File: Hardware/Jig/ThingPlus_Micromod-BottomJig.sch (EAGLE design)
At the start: 41 parts, among them J1 USB_A_PTH_MALE, J5 USB_A_SMT_FEMALE, J7 QWIIC_RIGHT_ANGLE, U1 TB_MAIN_BRAIN_CARDEDGE_TB_SIDE, U2 74LVC4066, U4 74LVC4066_MUX_1:1_X4

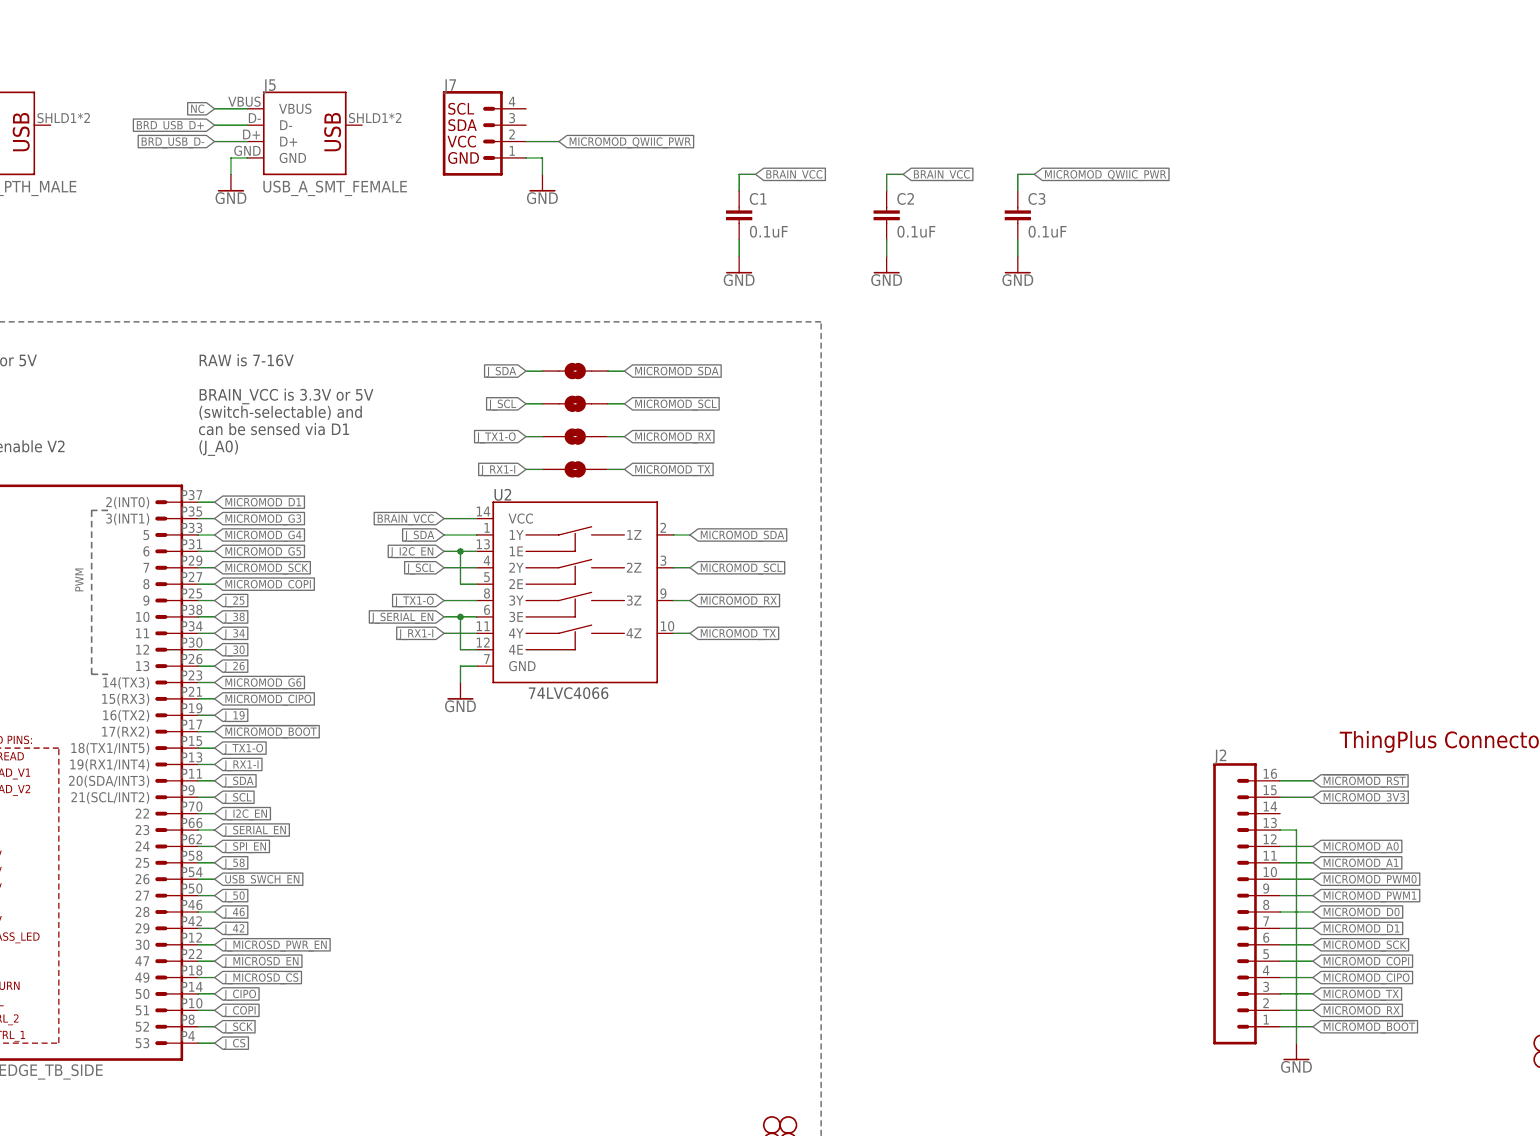
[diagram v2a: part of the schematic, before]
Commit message: Updated board and middle jig
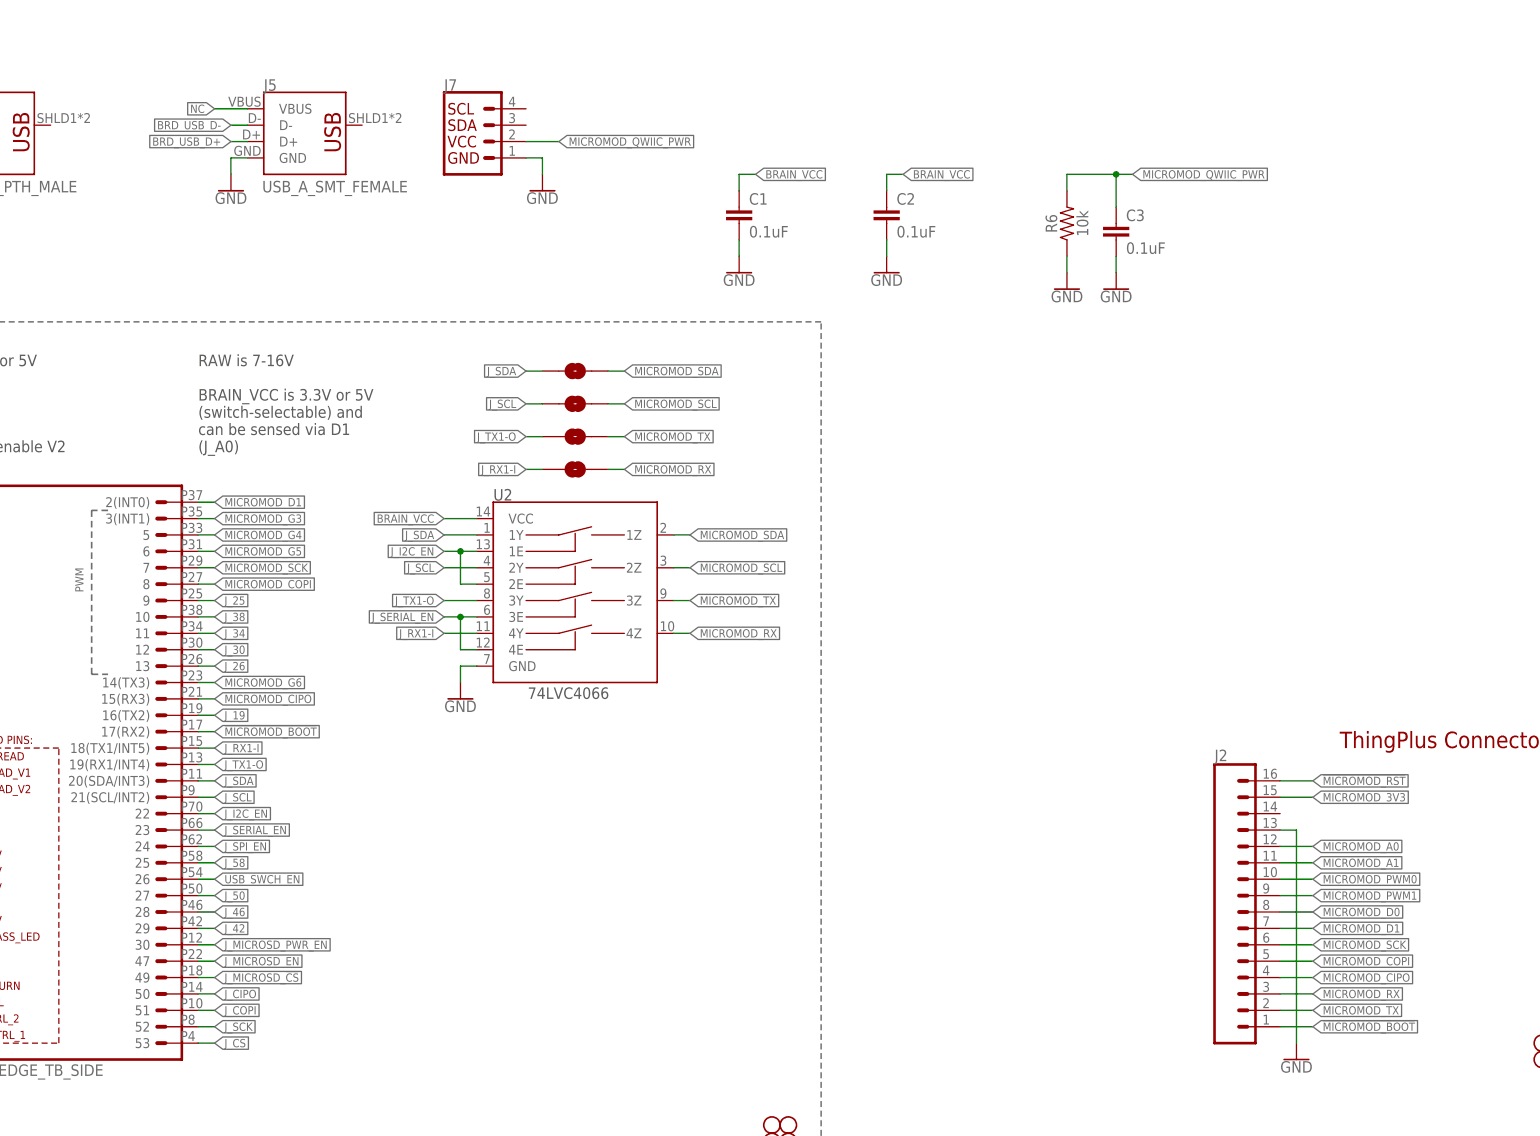
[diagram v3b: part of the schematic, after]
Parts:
- added R6: 10k, SparkFun-Resistors:10KOHM-0603-1/10W-1%
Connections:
- net BRD_USB_D+: now also J5.D+; no longer J5.D-
- net BRD_USB_D-: now also J5.D-; no longer J5.D+
- net GND: now also R6.1
- net J_RX1-I: now also U1.18(TX1/INT5); no longer U1.19(RX1/INT4)
- net J_TX1-O: now also U1.19(RX1/INT4); no longer U1.18(TX1/INT5)
- net MICROMOD_QWIIC_PWR: now also R6.2
- net MICROMOD_RX: now also J2.3, J_SDA.2, U2.4Z; no longer J2.2, J_SCL1.2, U2.3Z
- net MICROMOD_TX: now also J2.2, J_SCL1.2, U2.3Z; no longer J2.3, J_SDA.2, U2.4Z
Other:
- moved on the sheet: C3
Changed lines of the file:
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@@
 <part name="GND8" library="SparkFun-PowerSymbols" deviceset="GND" device=""/>
 <part name="H5" library="SparkFun-Hardware" deviceset="STAND-OFF" device=""/>
+<part name="R6" library="SparkFun-Resistors" deviceset="10KOHM" device="-0603-1/10W-1%" value="10k"/>
+<part name="GND9" library="SparkFun-PowerSymbols" deviceset="GND" device=""/>
 </parts>
 <sheets>
@@
 <attribute name="VALUE" x="264.16" y="187.706" size="1.778" layer="96" align="top-center"/>
 </instance>
-<instance part="C3" gate="G$1" x="284.48" y="195.58" smashed="yes">
-<attribute name="NAME" x="286.004" y="198.501" size="1.778" layer="95" font="vector"/>
-<attribute name="VALUE" x="286.004" y="193.421" size="1.778" layer="96" font="vector"/>
-</instance>
-<instance part="GND8" gate="1" x="284.48" y="187.96" smashed="yes">
-<attribute name="VALUE" x="284.48" y="187.706" size="1.778" layer="96" align="top-center"/>
+<instance part="C3" gate="G$1" x="299.72" y="193.04" smashed="yes">
+<attribute name="NAME" x="301.244" y="195.961" size="1.778" layer="95" font="vector"/>
+<attribute name="VALUE" x="301.244" y="190.881" size="1.778" layer="96" font="vector"/>
+</instance>
+<instance part="GND8" gate="1" x="299.72" y="185.42" smashed="yes">
+<attribute name="VALUE" x="299.72" y="185.166" size="1.778" layer="96" align="top-center"/>
 </instance>
 <instance part="H5" gate="G$1" x="246.38" y="55.88" smashed="yes"/>
+<instance part="R6" gate="G$1" x="292.1" y="195.58" smashed="yes" rot="R90">
+<attribute name="NAME" x="290.576" y="195.58" size="1.778" layer="95" font="vector" rot="R90" align="bottom-center"/>
+<attribute name="VALUE" x="293.624" y="195.58" size="1.778" layer="96" font="vector" rot="R90" align="top-center"/>
+</instance>
+<instance part="GND9" gate="1" x="292.1" y="185.42" smashed="yes">
+<attribute name="VALUE" x="292.1" y="185.166" size="1.778" layer="96" align="top-center"/>
+</instance>
 </instances>
 <busses>
@@
 <segment>
 <pinref part="C3" gate="G$1" pin="2"/>
-<wire x1="284.48" y1="193.04" x2="284.48" y2="190.5" width="0.1524" layer="91"/>
+<wire x1="299.72" y1="190.5" x2="299.72" y2="187.96" width="0.1524" layer="91"/>
 <pinref part="GND8" gate="1" pin="GND"/>
+</segment>
+<segment>
+<wire x1="292.1" y1="190.5" x2="292.1" y2="187.96" width="0.1524" layer="91"/>
+<pinref part="GND9" gate="1" pin="GND"/>
+<pinref part="R6" gate="G$1" pin="1"/>
 </segment>
 </net>
@@
 </segment>
 <segment>
-<label x="160.02" y="111.76" size="1.27" layer="95" xref="yes"/>
-<pinref part="U1" gate="G$1" pin="19(RX1/INT4)"/>
-<wire x1="157.48" y1="111.76" x2="160.02" y2="111.76" width="0.1524" layer="91"/>
+<pinref part="U1" gate="G$1" pin="18(TX1/INT5)"/>
+<wire x1="157.48" y1="114.3" x2="160.02" y2="114.3" width="0.1524" layer="91"/>
+<label x="160.02" y="114.3" size="1.27" layer="95" xref="yes"/>
 </segment>
 </net>
@@
 </segment>
 <segment>
-<label x="160.02" y="114.3" size="1.27" layer="95" xref="yes"/>
-<pinref part="U1" gate="G$1" pin="18(TX1/INT5)"/>
-<wire x1="157.48" y1="114.3" x2="160.02" y2="114.3" width="0.1524" layer="91"/>
+<pinref part="U1" gate="G$1" pin="19(RX1/INT4)"/>
+<wire x1="157.48" y1="111.76" x2="160.02" y2="111.76" width="0.1524" layer="91"/>
+<label x="160.02" y="111.76" size="1.27" layer="95" xref="yes"/>
 </segment>
 </net>
@@
 <segment>
 <pinref part="C3" gate="G$1" pin="1"/>
-<wire x1="284.48" y1="200.66" x2="284.48" y2="203.2" width="0.1524" layer="91"/>
-<wire x1="284.48" y1="203.2" x2="287.02" y2="203.2" width="0.1524" layer="91"/>
-<label x="287.02" y="203.2" size="1.27" layer="95" xref="yes"/>
+<wire x1="299.72" y1="198.12" x2="299.72" y2="203.2" width="0.1524" layer="91"/>
+<wire x1="299.72" y1="203.2" x2="302.26" y2="203.2" width="0.1524" layer="91"/>
+<label x="302.26" y="203.2" size="1.27" layer="95" xref="yes"/>
+<pinref part="R6" gate="G$1" pin="2"/>
+<wire x1="292.1" y1="200.66" x2="292.1" y2="203.2" width="0.1524" layer="91"/>
+<wire x1="292.1" y1="203.2" x2="299.72" y2="203.2" width="0.1524" layer="91"/>
+<junction x="299.72" y="203.2"/>
 </segment>
 </net>
@@
 </segment>
 <segment>
-<pinref part="J5" gate="G$1" pin="D-"/>
-<wire x1="165.1" y1="210.82" x2="160.02" y2="210.82" width="0.1524" layer="91"/>
-<label x="160.02" y="210.82" size="1.27" layer="95" rot="R180" xref="yes"/>
+<pinref part="J5" gate="G$1" pin="D+"/>
+<wire x1="165.1" y1="208.28" x2="162.56" y2="208.28" width="0.1524" layer="91"/>
+<label x="162.56" y="208.28" size="1.27" layer="95" rot="R180" xref="yes"/>
 </segment>
 </net>
@@
 </segment>
 <segment>
-<pinref part="J5" gate="G$1" pin="D+"/>
-<wire x1="165.1" y1="208.28" x2="160.02" y2="208.28" width="0.1524" layer="91"/>
-<label x="160.02" y="208.28" size="1.27" layer="95" rot="R180" xref="yes"/>
+<pinref part="J5" gate="G$1" pin="D-"/>
+<wire x1="165.1" y1="210.82" x2="162.56" y2="210.82" width="0.1524" layer="91"/>
+<label x="162.56" y="210.82" size="1.27" layer="95" rot="R180" xref="yes"/>
 </segment>
 </net>
@@
 </segment>
 </net>
-<net name="MICROMOD_RX" class="0">
+<net name="MICROMOD_TX" class="0">
 <segment>
 <pinref part="U2" gate="G$1" pin="3Z"/>
@@
 </segment>
 <segment>
+<pinref part="J_SCL1" gate="G$1" pin="2"/>
+<wire x1="223.52" y1="162.56" x2="220.98" y2="162.56" width="0.1524" layer="91"/>
+<label x="223.52" y="162.56" size="1.27" layer="95" xref="yes"/>
+</segment>
+<segment>
 <pinref part="J2" gate="G$1" pin="2"/>
 <wire x1="325.12" y1="73.66" x2="330.2" y2="73.66" width="0.1524" layer="91"/>
 <label x="330.2" y="73.66" size="1.27" layer="95" xref="yes"/>
 </segment>
-<segment>
-<pinref part="J_SCL1" gate="G$1" pin="2"/>
-<wire x1="223.52" y1="162.56" x2="220.98" y2="162.56" width="0.1524" layer="91"/>
-<label x="223.52" y="162.56" size="1.27" layer="95" xref="yes"/>
-</segment>
-</net>
-<net name="MICROMOD_TX" class="0">
+</net>
+<net name="MICROMOD_RX" class="0">
 <segment>
 <pinref part="U2" gate="G$1" pin="4Z"/>
